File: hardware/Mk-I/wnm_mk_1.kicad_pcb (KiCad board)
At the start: 2 copper layers, 100.9 x 62.4 mm, 123 parts, among them CON1 10118194-0001LF, SW1 EVQ-Q2S02W, SW10 EVQ-Q2S02W, SW11 EVQ-Q2S02W, SW12 EVQ-Q2S02W, SW13 EVQ-Q2S02W, SW14 EVQ-Q2S02W, SW15 EVQ-Q2S02W, SW16 EVQ-Q2S02W, SW2 EVQ-Q2S02W, SW20 EVQ-Q2S02W, SW21 EVQ-Q2S02W, SW22 EVQ-Q2S02W, SW3 EVQ-Q2S02W, SW4 EVQ-Q2S02W, SW5 EVQ-Q2S02W, SW6 EVQ-Q2S02W, SW7 EVQ-Q2S02W, SW8 EVQ-Q2S02W, SW9 EVQ-Q2S02W, U1 AP7313-18SRG-7, U10 STM32_SWD_Connector, U2 MCP73831T-2ACI/OT, U3 BD33IA5MEFJ-ME2, U4 STM32F427VIT6, U5 SGTL5000XNAA3R2, U6 EC12D1524403, U7 EC12D1524403, U8 Micro_SD_Card_Det_Hirose_DM3AT, U9 SSD1306, X1 ABM3B-8.000MHZ-B2-T

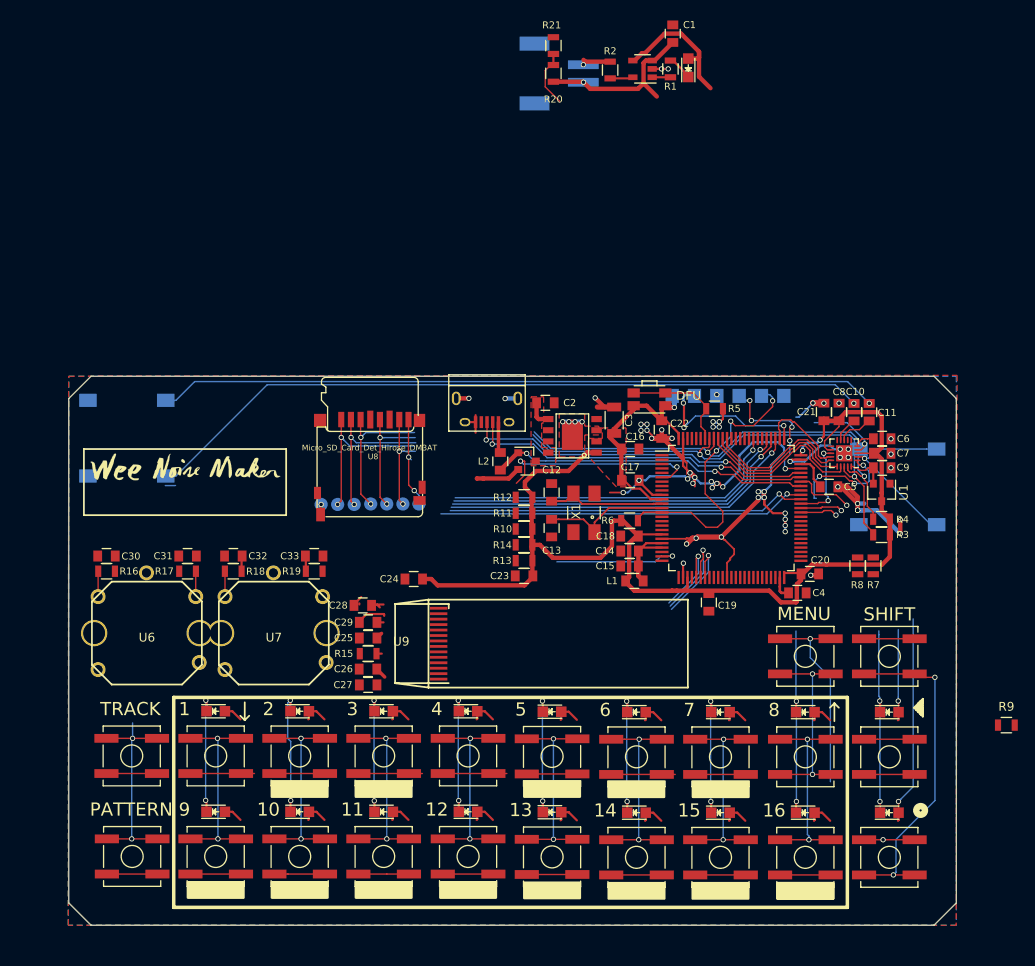
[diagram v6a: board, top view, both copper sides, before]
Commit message: HW: Change 3.5 socket and put them on top
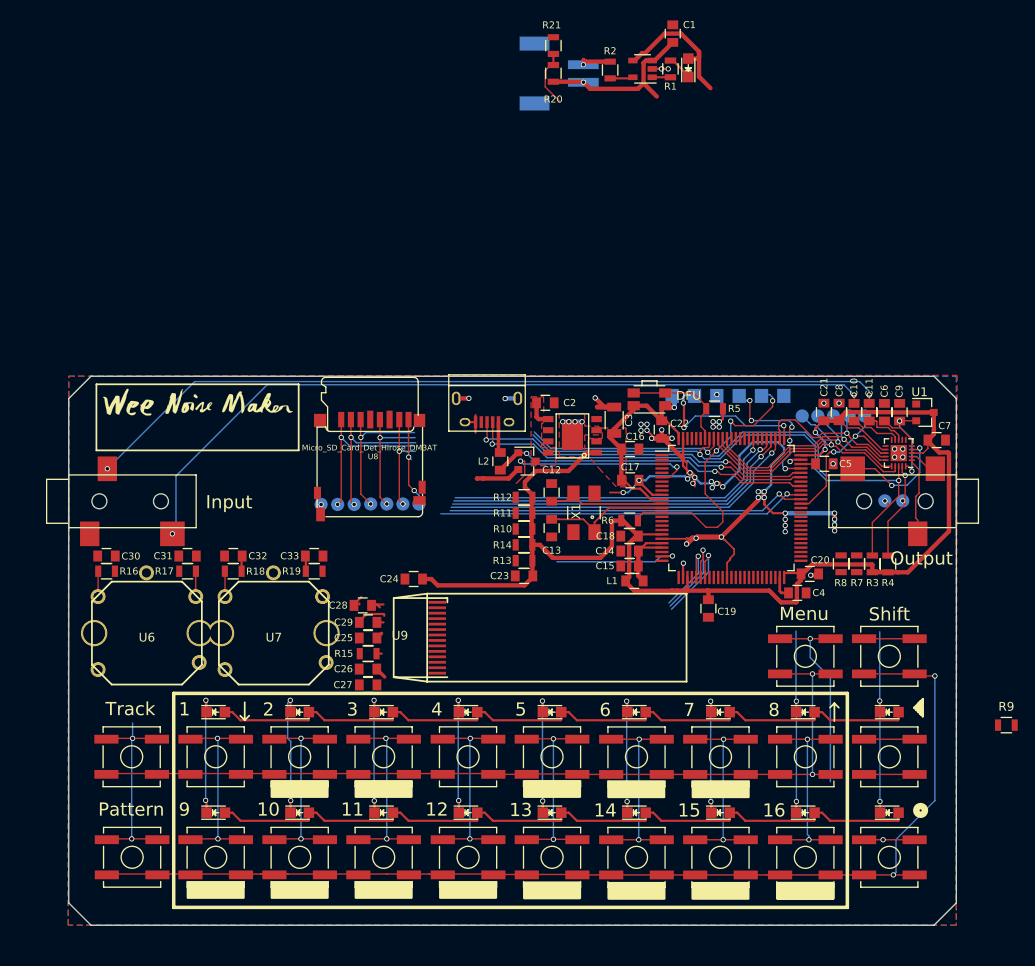
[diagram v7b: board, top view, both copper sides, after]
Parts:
- added TP_DIN1: TEST, Measurement_Points:Measurement_Point_Round-SMD-Pad_Small, B.Cu at (159.0, 84.3)
- added TP_DOUT1: TEST, Measurement_Points:Measurement_Point_Round-SMD-Pad_Small, B.Cu at (160.8, 84.3)
- added TP_LRCLK1: TEST, Measurement_Points:Measurement_Point_Round-SMD-Pad_Small, B.Cu at (164.3, 84.3)
- added TP_MCLK1: TEST, Measurement_Points:Measurement_Point_Round-SMD-Pad_Small, B.Cu at (166.1, 84.3)
- added TP_SCL1: TEST, Measurement_Points:Measurement_Point_Round-SMD-Pad_Small, B.Cu at (170.4, 94.0)
- added TP_SCLK1: TEST, Measurement_Points:Measurement_Point_Round-SMD-Pad_Small, B.Cu at (162.6, 84.3)
- added TP_SDA1: TEST, Measurement_Points:Measurement_Point_Round-SMD-Pad_Small, B.Cu at (168.4, 94.0)
- HP_OUT1, LINE_IN1: value 1503 02 -> SJ-3523-SMT; footprint POSS:lumberg_3.5_audio_jack_1503_02 -> POSS:SJ-3523-SMT; moved to F.Cu
- moved U1 10.4 mm to (173.0, 83.9), turned to 0 degrees
- moved G*** 7.50 mm to (90.3, 86.3)
- moved G*** 7.50 mm to (90.3, 82.8)
- moved C9 6.63 mm to (170.1, 83.9), turned to 90 degrees
- moved C7 6.38 mm to (174.3, 87.1)
- moved U5 6.20 mm to (170.0, 88.5)
- moved HP_OUT1 6.07 mm to (173.0, 94.0)
- moved R4 5.14 mm to (168.8, 101.2), turned to 90 degrees
- moved R3 3.46 mm to (167.0, 101.1), turned to 90 degrees
- moved LINE_IN1 3.16 mm to (79.1, 94.0)
- moved C6 3.03 mm to (168.4, 83.9), turned to 90 degrees
- moved C5 2.67 mm to (161.5, 89.8)
- moved R8 1.89 mm to (163.4, 101.1)
- moved R7 1.89 mm to (165.2, 101.1)
- moved C19 0.70 mm to (148.3, 106.2)
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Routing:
- net Net-(D10-Pad2): track 34.3 -> 86.7 mm, vias 1 -> 0
- net Net-(D1-Pad2): track 47.6 -> 86.7 mm, vias 1 -> 0
- net BUTTON_ROW2: track 90.1 -> 125.2 mm
- net BUTTON_ROW1: track 75.1 -> 99.5 mm
- net GND: track 141.3 -> 122.0 mm, vias 62 -> 57
- net 3V3: track 171.6 -> 190.4 mm
- net Net-(HP_OUT1-Pad2): track 21.3 -> 3.24 mm, vias 1 -> 0
- net Net-(C11-Pad1): track 81.9 -> 92.6 mm, vias 1 -> 2
- net I2S_DIN: track 19.7 -> 30.4 mm, vias 0 -> 1
- net I2S_DOUT: track 18.0 -> 27.8 mm, vias 0 -> 1
- net I2S_SCLK: track 16.8 -> 25.6 mm, vias 0 -> 1
- net I2S_MCLK: track 9.80 -> 18.2 mm
- net I2S_LRCLK: track 10.4 -> 18.4 mm, vias 0 -> 1
- net Audio_SCL: track 54.7 -> 62.2 mm, vias 2 -> 3
- net Audio_SDA: track 55.4 -> 62.3 mm, vias 2 -> 3
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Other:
- board text added: "DIN"
- board text added: "DOUT"
- board text added: "Input"
- board text added: "LRCLK"
- board text added: "MCLK"
- board text added: "Menu"
- board text added: "Output"
- board text added: "Pattern"
- board text added: "SCL"
- board text added: "SCLK"
- board text added: "SDA"
- board text added: "Shift"
- board text added: "Track"
- board text removed: "IN"
- board text removed: "MENU"
- board text removed: "OUT"
- board text removed: "PATTERN"
- board text removed: "SHIFT"
- board text removed: "TRACK"

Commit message: HW: Finish rev-D layout
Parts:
- removed R16, R17, R18, R19: 27K, Resistors_SMD:R_0805
- added TP_DBG_RX1: TEST, Measurement_Points:Measurement_Point_Round-SMD-Pad_Small, B.Cu at (162.6, 94.0)
- added TP_DBG_TX1: TEST, Measurement_Points:Measurement_Point_Round-SMD-Pad_Small, B.Cu at (160.3, 94.0)
- moved C1 62.8 mm to (120.0, 98.8), turned to 270 degrees
- moved R2 55.9 mm to (122.0, 98.8), turned to 90 degrees
- moved U2 53.1 mm to (121.2, 94.2), turned to 270 degrees
- moved R21 53.0 mm to (124.7, 94.9), turned to 90 degrees
- moved R1 51.5 mm to (121.2, 91.0), turned to 180 degrees
- moved R9 51.2 mm to (133.9, 102.5), turned to 180 degrees
- moved BAT1 50.8 mm to (121.0, 89.0), turned to 0 degrees
- moved BT1 47.0 mm to (113.1, 88.7), turned to 180 degrees
- moved R20 46.9 mm to (124.7, 91.8), turned to 90 degrees
- moved C23 24.3 mm to (103.5, 98.1)
- moved R12 20.7 mm to (107.1, 97.8), turned to 90 degrees
- moved R11 18.7 mm to (108.8, 97.8), turned to 90 degrees
- moved R10 16.8 mm to (110.6, 97.8), turned to 90 degrees
- moved C24 15.2 mm to (117.4, 87.9), turned to 270 degrees
- moved R14 15.0 mm to (112.4, 97.8), turned to 90 degrees
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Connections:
- net B10 renamed Net-(U4-Pad26)
- net ENC_1_SW renamed Net-(U4-Pad8)
- net ENC_2_SW renamed Net-(U4-Pad9)
- CON1 pad 4: Net-(CON1-Pad4) -> FS_ID
- U4 pad 15: COL1 -> Net-(U4-Pad15)
- U4 pad 17: COL2 -> Net-(U4-Pad17)
- U4 pad 23: PLAY_WAKEUP -> Play_WKUP
- U4 pad 24: ENC_1_B -> ENC_2_A
- U4 pad 25: Net-(U4-Pad25) -> BUTTON_ROW3
- U4 pad 29: COL3 -> Screen_Nreset
- U4 pad 30: ENC_1_A -> ENC_2_B
- U4 pad 31: ENC_2_A -> ENC_1_B
- U4 pad 32: ENC_2_B -> ENC_1_A
- U4 pad 33: Net-(U4-Pad33) -> BUTTON_COL1
- U4 pad 34: Net-(U4-Pad34) -> COL1
- U4 pad 35: COL4 -> BUTTON_COL2
- U4 pad 36: Net-(U4-Pad36) -> COL2
- U4 pad 38: Net-(U4-Pad38) -> BUTTON_COL3
- U4 pad 39: Net-(U4-Pad39) -> COL3
- U4 pad 40: COL5 -> BUTTON_COL4
- U4 pad 41: Net-(U4-Pad41) -> COL4
- U4 pad 42: Net-(U4-Pad42) -> BUTTON_COL5
- U4 pad 43: Net-(U4-Pad43) -> COL5
- U4 pad 44: COL6 -> BUTTON_COL6
- U4 pad 45: Net-(U4-Pad45) -> COL6
- U4 pad 46: Net-(U4-Pad46) -> BUTTON_COL7
- U4 pad 47: Net-(U4-Pad47) -> COL7
- U4 pad 48: COL7 -> BUTTON_COL8
- U4 pad 51: Net-(U4-Pad51) -> BUTTON_ROW1
- U4 pad 52: Net-(U4-Pad52) -> COL8
- U4 pad 53: Net-(U4-Pad53) -> BUTTON_COL9
- U4 pad 54: COL8 -> BUTTON_COL10
- U4 pad 55: Net-(U4-Pad55) -> DBG_TX
- U4 pad 56: Net-(U4-Pad56) -> DBG_RX
- U4 pad 57: Net-(U4-Pad57) -> BUTTON_COL11
- U4 pad 58: Net-(U4-Pad58) -> COL9
- U4 pad 61: COL9 -> BUTTON_ROW2
- U4 pad 69: Write -> FS_ID
- U4 pad 7: Screen_NReset -> Net-(U4-Pad7)
- U6 pad 1: Net-(R16-Pad1) -> ENC_1_A
- U6 pad 2: Net-(R17-Pad2) -> ENC_1_B
- U6 pad 6: (no net) -> GND
- U7 pad 1: Net-(R18-Pad1) -> ENC_2_A
- U7 pad 2: Net-(R19-Pad2) -> ENC_2_B
- U7 pad 6: (no net) -> GND
- U9 pad 9: Screen_NReset -> Screen_Nreset
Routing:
- net 3V3: track 190.4 -> 268.5 mm, vias 3 -> 5
- net BUTTON_COL1: track 24.7 -> 98.8 mm, vias 2 -> 3
- net BUTTON_COL2: track 23.0 -> 95.2 mm, vias 2 -> 3
- net ENC_1_A: track 9.21 -> 80.1 mm
- net BUTTON_COL3: track 22.9 -> 90.8 mm, vias 2 -> 3
- net COL1: track 14.0 -> 81.1 mm, vias 2 -> 3
- net COL2: track 14.2 -> 77.3 mm, vias 2 -> 3
- net Play_WKUP: track 5.75 -> 66.6 mm, vias 0 -> 3
- net BUTTON_ROW3: track 0.00 -> 59.2 mm, vias 0 -> 1
- net COL3: track 14.0 -> 69.8 mm, vias 2 -> 3
- net BUTTON_COL4: track 23.0 -> 78.2 mm, vias 2 -> 3
- net ENC_1_B: track 14.6 -> 69.2 mm
- net COL4: track 14.0 -> 61.4 mm, vias 2 -> 3
- net BUTTON_COL5: track 23.0 -> 69.8 mm, vias 2 -> 3
- net ENC_2_A: track 12.9 -> 58.4 mm
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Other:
- board text added: "Func"
- board text added: "RX"
- board text added: "TX"
- board text removed: "Input"
- board text removed: "Output"
- board text removed: "SWO"
- board text removed: "Shift"
